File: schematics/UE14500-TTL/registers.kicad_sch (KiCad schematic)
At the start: 10 parts, among them U10 74LS74, U11 74LS00, U2 74LS08, U7 74LS74, U8 74LS02, U9 74LS02

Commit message: Lay out CPU board
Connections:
- net CAR_VAL renamed CAR_ALU
- net RR_VAL renamed RR_ALU
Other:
- note added: "Latch downstream regisers and memory on the falling edge of WRITE."
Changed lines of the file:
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@@
+		)
+	)
+	(text "Latch downstream regisers and memory\non the falling edge of WRITE."
+		(exclude_from_sim no)
+		(at 232.156 140.208 0)
+		(effects
+			(font
+				(size 1.27 1.27)
+			)
+			(justify left)
 		)
 	)
@@
 		)
 	)
-	(global_label "RR_VAL"
+	(global_label "RR_ALU"
 		(shape input)
 		(at 71.12 55.88 180)
@@
 		)
 		(property "Intersheetrefs" "${INTERSHEET_REFS}"
-			(at 61.4219 55.88 0)
+			(at 61.18 55.88 0)
 			(effects
 				(font
@@
 		)
 	)
-	(global_label "CAR_VAL"
+	(global_label "CAR_ALU"
 		(shape input)
 		(at 71.12 101.6 180)
@@
 		)
 		(property "Intersheetrefs" "${INTERSHEET_REFS}"
-			(at 60.3333 101.6 0)
-			(effects
-				(font
+			(at 60.0914 101.6 0)
+			(effects
+				(font

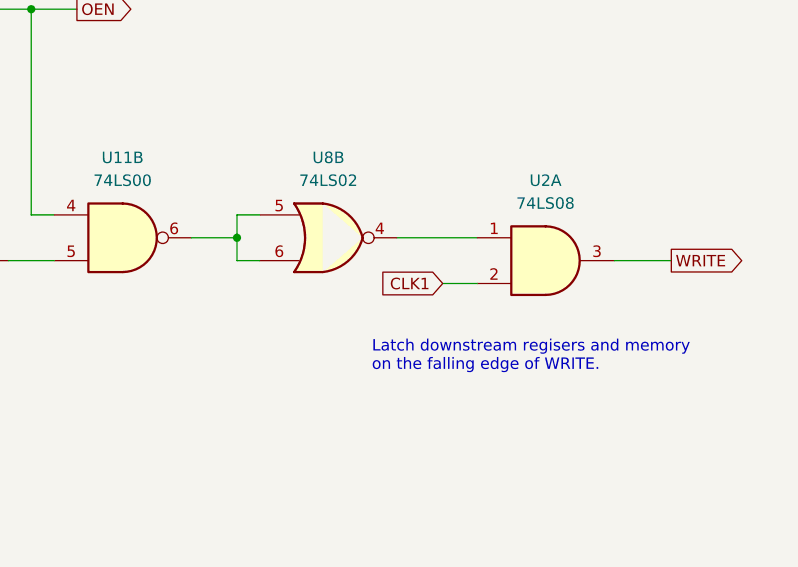
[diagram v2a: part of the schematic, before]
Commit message: Fix WRITE gating on processor board
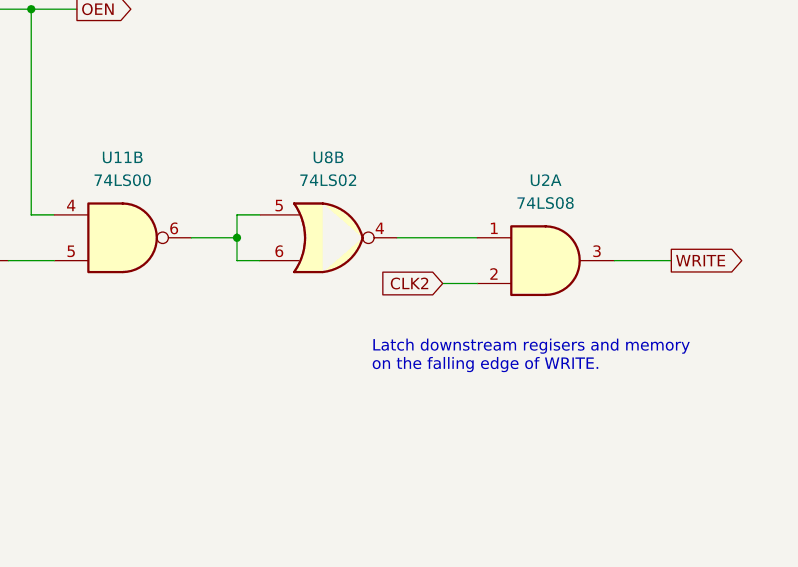
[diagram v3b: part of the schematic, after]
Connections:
- net CLK1: no longer U2.2
- new net CLK2: U2.2
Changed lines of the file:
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@@
 		)
 	)
-	(global_label "CLK1"
+	(global_label "CLK2"
 		(shape input)
 		(at 240.03 132.08 180)
